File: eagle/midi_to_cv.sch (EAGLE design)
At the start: 66 parts, among them IC1 4093N, Q3 2N3904, Q4 2N3904, Q5 2N3904, Q6 2SK30, U1 ATMEGA328P_PDIP

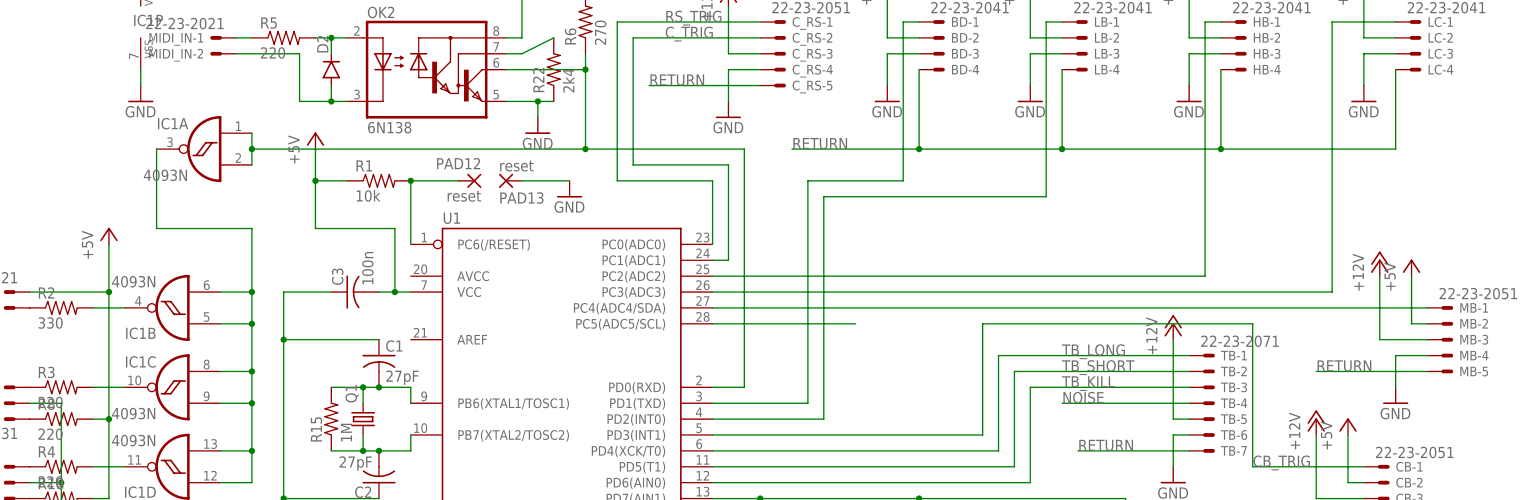
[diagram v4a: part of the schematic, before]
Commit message: shifted accent pin closer to circuit
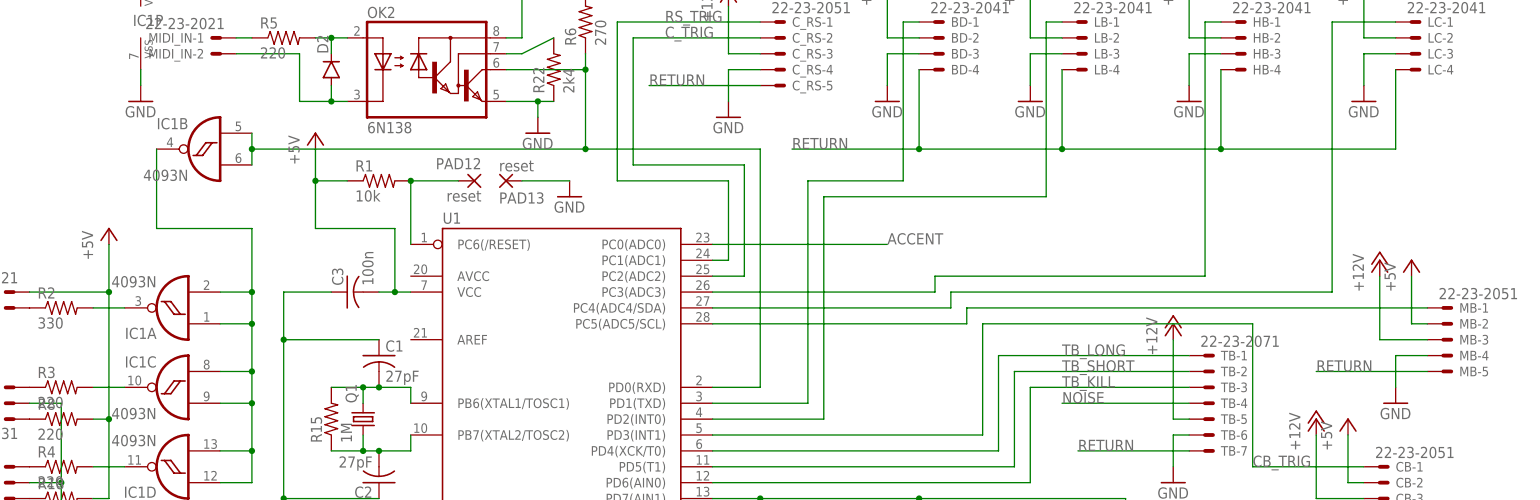
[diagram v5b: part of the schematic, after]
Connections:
- net ACCENT: now also U1.PC0(ADC0); no longer U1.PC5(ADC5/SCL)
- net C_TRIG: now also U1.PC2(ADC2); no longer U1.PC1(ADC1)
- net N$11: now also IC1B.I0, IC1B.I1; no longer IC1A.I0, IC1A.I1
- net N$12: now also IC1A.O; no longer IC1B.O
- net N$14: now also U1.PC3(ADC3); no longer U1.PC2(ADC2)
- net N$24: now also U1.PC5(ADC5/SCL); no longer U1.PC4(ADC4/SDA)
- net N$25: now also U1.PC4(ADC4/SDA); no longer U1.PC3(ADC3)
- net N$30: now also IC1A.I0, IC1A.I1, IC1B.O; no longer IC1A.O, IC1B.I0, IC1B.I1
- net RS_TRIG: now also U1.PC1(ADC1); no longer U1.PC0(ADC0)
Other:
- moved on the sheet: IC1A, IC1B

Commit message: tweaks toward auto
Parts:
- R15: device rcl:R-US_0207/10 -> rcl:R-US_0204/7
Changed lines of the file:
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@@
 <part name="C6" library="rcl" deviceset="C-US" device="050-024X044" value="100n"/>
 <part name="C7" library="rcl" deviceset="C-US" device="050-024X044" value="100n"/>
-<part name="R15" library="rcl" deviceset="R-US_" device="0207/10" value="1M"/>
+<part name="R15" library="rcl" deviceset="R-US_" device="0204/7" value="1M"/>
 <part name="OK2" library="optocoupler" deviceset="6N138" device=""/>
 <part name="D2" library="SparkFun-DiscreteSemi" deviceset="DIODE" device="1N4148"/>

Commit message: 96pct auto
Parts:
- R1: device rcl:R-US_0204/7 -> rcl:R-US_0204/5
- R12: device rcl:R-US_0207/12 -> rcl:R-US_0207/15
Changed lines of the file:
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@@
 <part name="C1" library="rcl" deviceset="C-US" device="025-040X050" value="27pF"/>
 <part name="C2" library="rcl" deviceset="C-US" device="025-040X050" value="27pF"/>
-<part name="R1" library="rcl" deviceset="R-US_" device="0204/7" value="10k"/>
+<part name="R1" library="rcl" deviceset="R-US_" device="0204/5" value="10k"/>
 <part name="C3" library="rcl" deviceset="C-US" device="025-040X050" value="100n"/>
 <part name="P+1" library="supply1" deviceset="+5V" device=""/>
@@
 <part name="P+7" library="supply1" deviceset="+12V" device=""/>
 <part name="R11" library="rcl" deviceset="R-US_" device="0204/7" value="15k"/>
-<part name="R12" library="rcl" deviceset="R-US_" device="0207/12" value="47k"/>
+<part name="R12" library="rcl" deviceset="R-US_" device="0207/15" value="47k"/>
 <part name="C9" library="rcl" deviceset="C-US" device="050-025X075" value="18p"/>
 <part name="R13" library="rcl" deviceset="R-US_" device="0204/7" value="100k"/>

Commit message: routed
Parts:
- D1: device SparkFun-DiscreteSemi:DIODE1N4148 -> SparkFun-DiscreteSemi:DIODEKIT
- R1: device rcl:R-US_0204/5 -> rcl:R-US_0204/7
- R12: device rcl:R-US_0207/15 -> rcl:R-US_0207/12
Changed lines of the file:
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@@
 <part name="C1" library="rcl" deviceset="C-US" device="025-040X050" value="27pF"/>
 <part name="C2" library="rcl" deviceset="C-US" device="025-040X050" value="27pF"/>
-<part name="R1" library="rcl" deviceset="R-US_" device="0204/5" value="10k"/>
+<part name="R1" library="rcl" deviceset="R-US_" device="0204/7" value="10k"/>
 <part name="C3" library="rcl" deviceset="C-US" device="025-040X050" value="100n"/>
 <part name="P+1" library="supply1" deviceset="+5V" device=""/>
@@
 <part name="P+7" library="supply1" deviceset="+12V" device=""/>
 <part name="R11" library="rcl" deviceset="R-US_" device="0204/7" value="15k"/>
-<part name="R12" library="rcl" deviceset="R-US_" device="0207/15" value="47k"/>
+<part name="R12" library="rcl" deviceset="R-US_" device="0207/12" value="47k"/>
 <part name="C9" library="rcl" deviceset="C-US" device="050-025X075" value="18p"/>
 <part name="R13" library="rcl" deviceset="R-US_" device="0204/7" value="100k"/>
 <part name="GND10" library="supply1" deviceset="GND" device=""/>
-<part name="D1" library="SparkFun-DiscreteSemi" deviceset="DIODE" device="1N4148"/>
+<part name="D1" library="SparkFun-DiscreteSemi" deviceset="DIODE" device="KIT"/>
 <part name="C10" library="rcl" deviceset="C-US" device="025-040X050" value="47n"/>
 <part name="GND11" library="supply1" deviceset="GND" device=""/>
